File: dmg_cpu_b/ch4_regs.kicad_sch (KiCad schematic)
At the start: 91 parts

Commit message: Fixes made from issues, channel 4 sheet aded and tidy up of hierarchical APU sheet. Small fixes done here and there when doing ERC.
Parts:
- added ATEL: TRI_INV_IF0, symbol DMG_CPU_Cells:TRI_INV_IF0
- added BAGU: NAND_2, symbol DMG_CPU_Cells:NAND_2
- added BEFA, CEPY, COSA: INVERTER_A, symbol DMG_CPU_Cells:INVERTER_A
- added COMO, COTE, DYRY: AND_2, symbol DMG_CPU_Cells:AND_2
- renumbered KUKO to KOKU
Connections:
- net D0: now also ATEL.3
- net FF23: now also BAGU.1
- net FF23_D6: now also CEPY.1
- net ~{CPU_RD}: now also COSA.1
- net ~{FF23_D6}: no longer CUNY.6 (~{Q}), CURY.2
- net at FEXO.2, GARU.4 (~{RESET}), GEDU.4 (~{RESET})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: now also EMOK.4 (~{RESET}), ETYJ.4 (~{RESET}), EZYK.4 (~{RESET})
- new net: CEPY.2, COTE.1, DYRY.1
- new net: CUNY.6 (~{Q}), CURY.2
- new net: ATEL.1 (~{ENA}), BAGU.3
- new net: ATEL.2, BEFA.2
- new net: COMO.2, COSA.2
- new net: BAGU.2, COMO.3
- new net CH4_EG_TEST: COTE.3
- new net NET03: COTE.2, DYRY.2
- new net NOISE_COUNTER_BYPASS: COMO.1, DYRY.3
- new net NOISE_COUNTER_CLK: BEFA.1
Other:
- moved on the sheet: BARE, BOXE, BYLO, CABE, CAZE, CEDO, CUNY, CURY, CUWA, DANO, DENA, DODA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

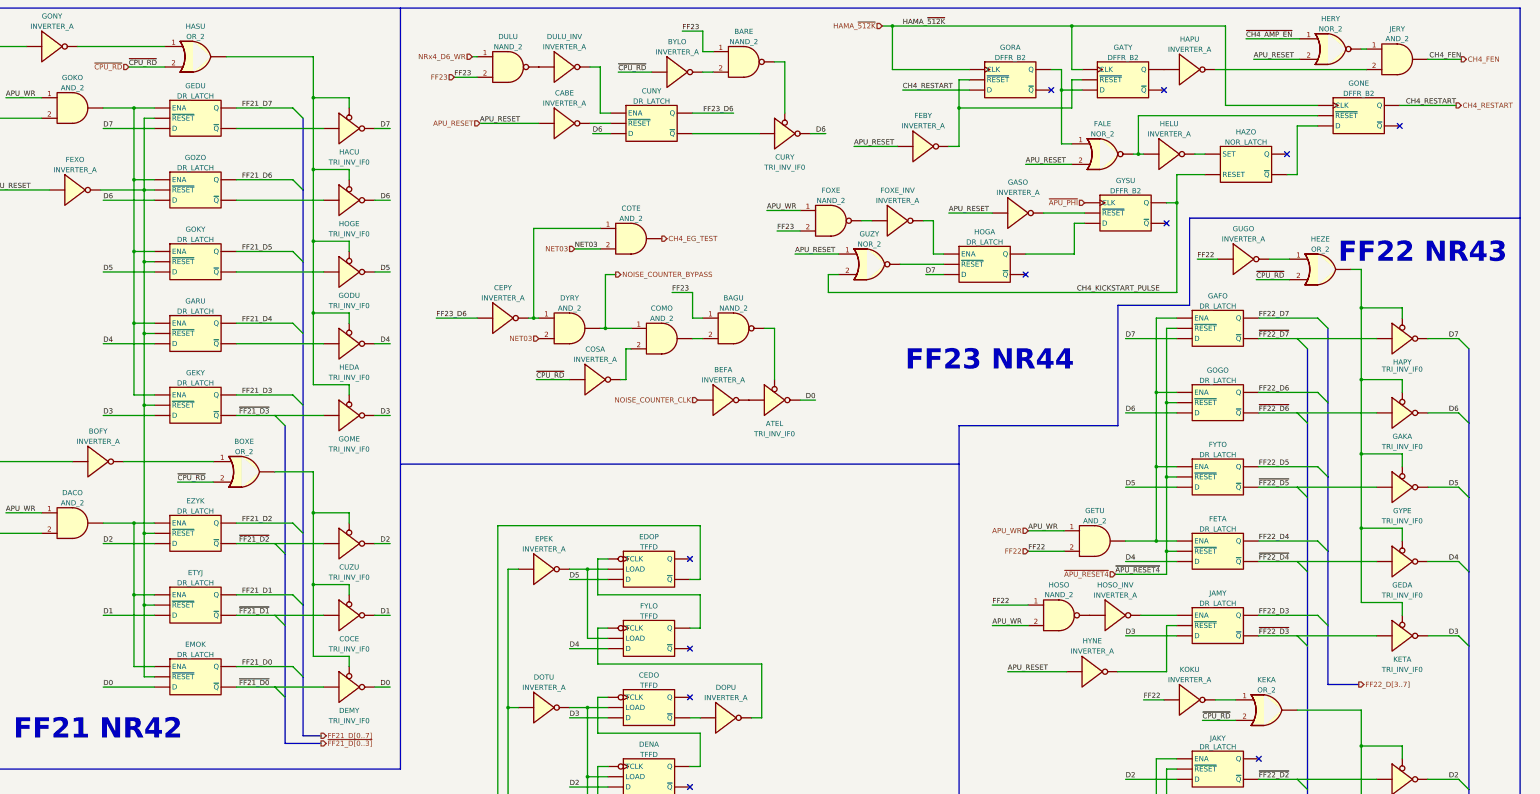
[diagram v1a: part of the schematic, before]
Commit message: Fixes made based on raised issues. PPU decode page added as draft level.
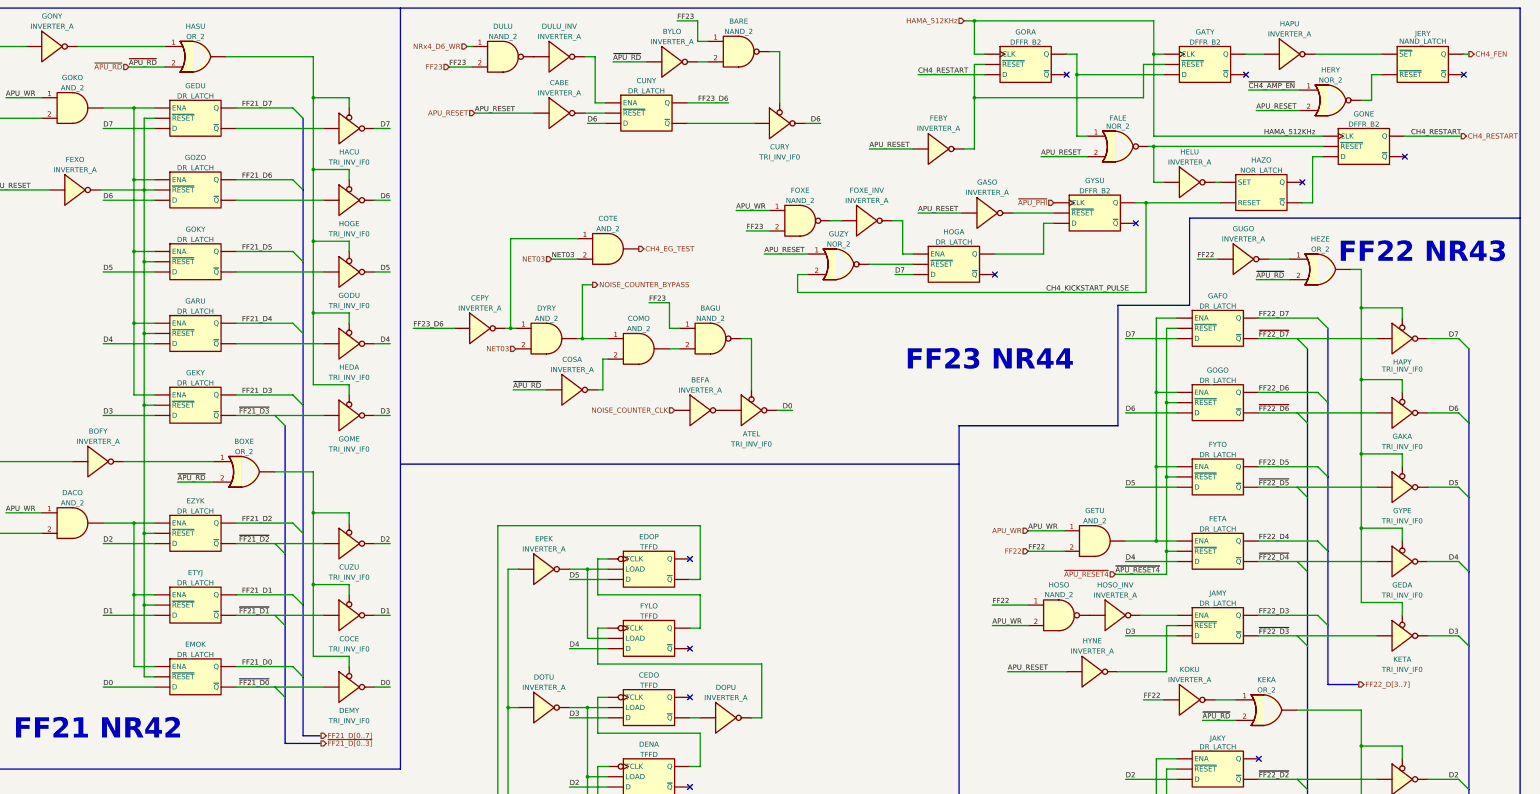
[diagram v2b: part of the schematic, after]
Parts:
- JERY: value AND_2 -> NAND_LATCH; symbol DMG_CPU_Cells:AND_2 -> DMG_CPU_Cells:NAND_LATCH
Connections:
- net at JERY.2 (~{Q}): no longer HAPU.2
- net HAMA_~{512K} renamed HAMA_512KHz
- net ~{CPU_RD} renamed ~{APU_RD}
- new net: HAPU.2, JERY.4 (~{SET})
- no-connect marks 16 -> 17
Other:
- moved on the sheet: ATEL, BAGU, BARE, BEFA, BYLO, CABE, CEPY, COMO, COSA, COTE, CUNY, CURY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

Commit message: Further fixes made based on raised issues.
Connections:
- net CH4_FDIS: now reaches JERY.2 (~{Q})
- net CH4_FEN: no longer names the net of JERY.3 (Q)
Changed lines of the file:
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@@
   (junction (at 173.99 95.25) (diameter 0) (color 0 0 0 0)
   )
-  (no_connect (at 392.43 29.845))
+  (no_connect (at 392.43 24.765))
   (no_connect (at 200.66 206.375))
   (no_connect (at 200.66 184.15))
@@
     (stroke (width 0) (type default) (color 0 0 0 0))
   )
-  (wire (pts (xy 393.7 24.765) (xy 392.43 24.765))
+  (wire (pts (xy 394.97 29.845) (xy 392.43 29.845))
     (stroke (width 0) (type default) (color 0 0 0 0))
   )
@@
     (effects (font (size 1.27 1.27)) (justify right))
   )
-  (hierarchical_label "CH4_FEN" (shape output) (at 393.7 24.765 0)
+  (hierarchical_label "CH4_FDIS" (shape output) (at 394.97 29.845 0)
     (effects (font (size 1.27 1.27)) (justify left))
   )

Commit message: Fixes made based on raised issues (in APU sheets).
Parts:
- added JORA: NAND_2, symbol DMG_CPU_Cells:NAND_2
- added KAGE: INVERTER_A, symbol DMG_CPU_Cells:INVERTER_A
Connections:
- net APU_RESET: now also FALE.1; no longer FALE.2
- net APU_WR: now also GOKO.2; no longer GOKO.1
- net FF21: now also GOKO.1; no longer GOKO.2
- net FF22: now also JORA.2
- net FF23_D6: now also DYRY.1, EFOT.1; no longer EFOT.2
- net ~{APU_RD}: now also KAGE.1
- net ~{FF23_D6}: now also CUNY.6 (~{Q}), CURY.2
- net at GAKA.1 (~{ENA}), GEDA.1 (~{ENA}), GYPE.1 (~{ENA})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: no longer KETA.1 (~{ENA})
- net at DODA.1, FUGO.6 (Q): now also EFOT.2; no longer EFOT.1
- net at GATY.3 (D), GORA.6 (Q): now also FALE.2; no longer FALE.1
- net at CEPY.2, COTE.1: no longer DYRY.1
- net ~{FF22_D7}: no longer names the net of GAFO.6 (~{Q}), HAPY.2
- new net: JORA.3, KETA.1 (~{ENA})
- new net: JORA.1, KAGE.2
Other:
- moved on the sheet: CEPY, COTE, FETA, FYTO, GAKA, GEDA, GETU, GOGO, GYPE, HOSO, HOSO_INV, HYNE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

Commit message: VRAM interface sheet added but various edits in existing sheets. Notable merge of RESET, CLOCKS and FF04 DIV sheets
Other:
- company: (none) -> CC-BY-SA-4.0 Régis Galland & Michael Singer -- Derived work from Furrtek
- title: (none) -> DMG CPU B
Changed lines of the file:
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@@
 (kicad_sch (version 20211123) (generator eeschema)
   (paper "A3")
+  (title_block
+    (title "DMG CPU B")
+    (date "2022-05-02")
+    (rev "0")
+    (company "CC-BY-SA-4.0 Régis Galland & Michael Singer -- Derived work from Furrtek")
+    (comment 1 "https://github.com/msinger/dmg-schematics")
+  )
   (junction (at 211.455 254) (diameter 0) (color 0 0 0 0)
   )

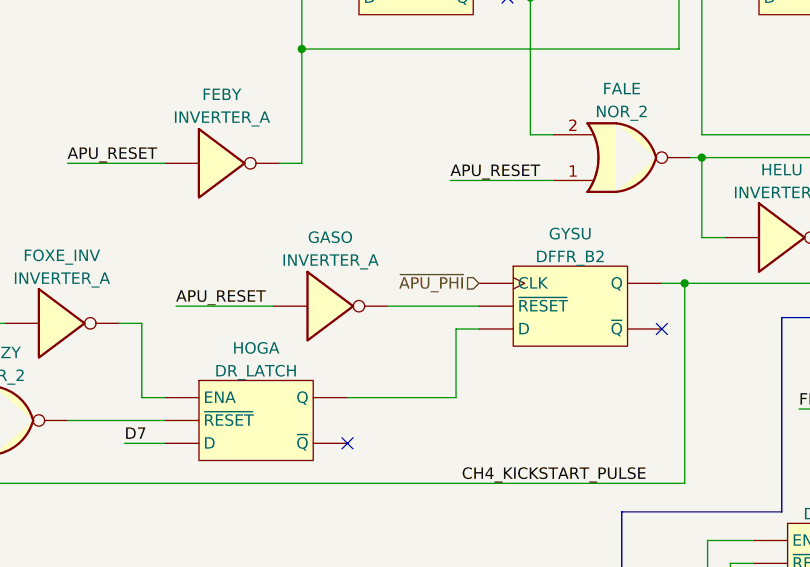
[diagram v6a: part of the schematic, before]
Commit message: Fixed PHI signals.
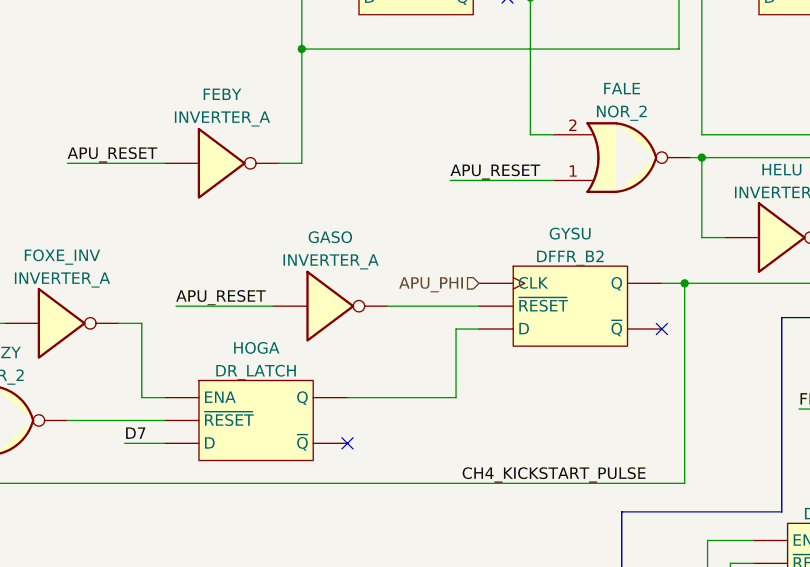
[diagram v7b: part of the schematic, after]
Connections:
- net ~{APU_PHI} renamed APU_PHI
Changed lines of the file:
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@@
     (effects (font (size 1.27 1.27)) (justify left))
   )
-  (hierarchical_label "~{APU_PHI}" (shape input) (at 290.83 61.595 180)
+  (hierarchical_label "APU_PHI" (shape input) (at 290.83 61.595 180)
     (effects (font (size 1.27 1.27)) (justify right))
   )
